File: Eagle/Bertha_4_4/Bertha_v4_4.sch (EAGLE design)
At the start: 115 parts, among them CON1 JACK_DC_BARREL, CON2 JACK_DC_BARREL, IC1 MCP1703DB, J1 RJ12RIGHTANGLE-I2C, J2 RJ12RIGHTANGLE-I2C, Q1 BSP75, Q2 BSP75, Q3 BSP75, Q4 BSP75, Q5 BSP75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

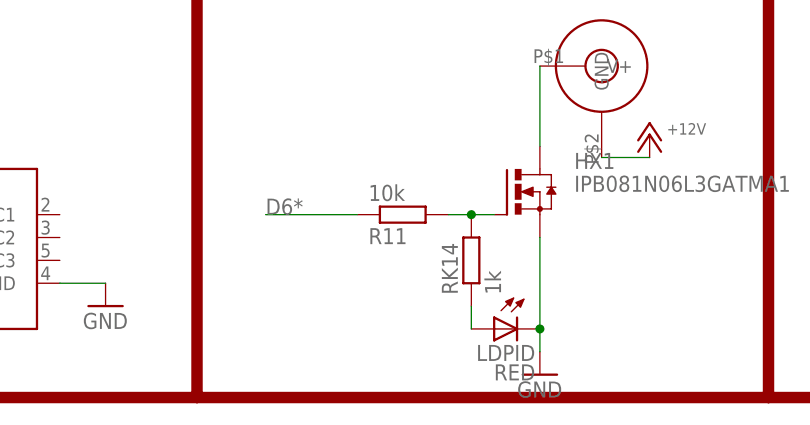
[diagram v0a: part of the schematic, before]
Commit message: correted PID diode, 4.5 finished, closes #72, ref #47
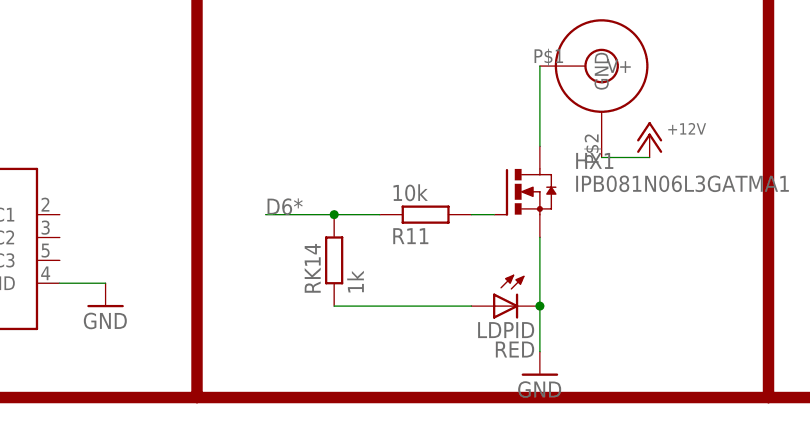
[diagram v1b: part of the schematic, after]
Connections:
- removed net N$6: HX1.G, R11.2, RK14.2
- new net N$4: HX1.G, R11.2
- net D6*: now also RK14.2
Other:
- moved on the sheet: LDPID, R11, RK14
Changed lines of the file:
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@@
 <?xml version="1.0" encoding="utf-8"?>
 <!DOCTYPE eagle SYSTEM "eagle.dtd">
-<eagle version="7.5.0">
+<eagle version="6.5.0">
 <drawing>
 <settings>
@@
 <instance part="GND27" gate="1" x="337.82" y="266.7"/>
 <instance part="HX1" gate="G$1" x="358.14" y="30.48"/>
-<instance part="R11" gate="G$1" x="345.44" y="27.94" rot="MR180"/>
+<instance part="R11" gate="G$1" x="347.98" y="27.94" rot="MR180"/>
 <instance part="P+2" gate="1" x="372.872" y="36.83" smashed="yes">
 <attribute name="VALUE" x="374.777" y="36.83" size="1.27" layer="96"/>
@@
 <instance part="Q6" gate="G$1" x="78.74" y="53.34"/>
 <instance part="Q5" gate="G$1" x="78.74" y="27.94"/>
-<instance part="RK14" gate="G$1" x="353.06" y="22.86" rot="R90"/>
+<instance part="RK14" gate="G$1" x="337.82" y="22.86" rot="R90"/>
 <instance part="RK13" gate="G$1" x="68.58" y="20.32" rot="R90"/>
 <instance part="RK12" gate="G$1" x="71.12" y="45.72" rot="R90"/>
@@
 <instance part="P+7" gate="G$1" x="487.68" y="274.32"/>
 <instance part="GND66" gate="1" x="487.68" y="264.16"/>
-<instance part="LDPID" gate="G$1" x="355.6" y="15.24" rot="MR270"/>
+<instance part="LDPID" gate="G$1" x="355.6" y="17.78" rot="MR270"/>
 <instance part="STEPPER" gate="G$1" x="497.84" y="119.38" rot="R180"/>
 <instance part="LDIN" gate="G$1" x="76.2" y="40.64" rot="MR270"/>
@@
 <pinref part="HX1" gate="G$1" pin="S"/>
 <pinref part="GND2" gate="1" pin="GND"/>
-<wire x1="360.68" y1="25.4" x2="360.68" y2="15.24" width="0.1524" layer="91"/>
+<wire x1="360.68" y1="25.4" x2="360.68" y2="17.78" width="0.1524" layer="91"/>
 <pinref part="LDPID" gate="G$1" pin="C"/>
-<wire x1="360.68" y1="15.24" x2="360.68" y2="12.7" width="0.1524" layer="91"/>
-<junction x="360.68" y="15.24"/>
+<wire x1="360.68" y1="17.78" x2="360.68" y2="12.7" width="0.1524" layer="91"/>
+<junction x="360.68" y="17.78"/>
 </segment>
 <segment>
@@
 <segment>
 <pinref part="R11" gate="G$1" pin="1"/>
-<wire x1="340.36" y1="27.94" x2="330.2" y2="27.94" width="0.1524" layer="91"/>
+<wire x1="342.9" y1="27.94" x2="337.82" y2="27.94" width="0.1524" layer="91"/>
 <label x="330.2" y="27.94" size="1.778" layer="95"/>
+<pinref part="RK14" gate="G$1" pin="2"/>
+<wire x1="337.82" y1="27.94" x2="330.2" y2="27.94" width="0.1524" layer="91"/>
+<junction x="337.82" y="27.94"/>
 </segment>
 </net>
@@
 </segment>
 </net>
-<net name="N$6" class="0">
-<segment>
-<pinref part="R11" gate="G$1" pin="2"/>
-<pinref part="HX1" gate="G$1" pin="G"/>
-<wire x1="350.52" y1="27.94" x2="353.06" y2="27.94" width="0.1524" layer="91"/>
-<pinref part="RK14" gate="G$1" pin="2"/>
-<wire x1="353.06" y1="27.94" x2="355.6" y2="27.94" width="0.1524" layer="91"/>
-<junction x="353.06" y="27.94"/>
-</segment>
-</net>
 <net name="N$3" class="0">
 <segment>
@@
 <segment>
 <pinref part="RK14" gate="G$1" pin="1"/>
-<wire x1="353.06" y1="15.24" x2="353.06" y2="17.78" width="0.1524" layer="91"/>
+<wire x1="353.06" y1="17.78" x2="337.82" y2="17.78" width="0.1524" layer="91"/>
 <pinref part="LDPID" gate="G$1" pin="A"/>
 </segment>
@@
 </segment>
 </net>
+<net name="N$4" class="0">
+<segment>
+<pinref part="HX1" gate="G$1" pin="G"/>
+<pinref part="R11" gate="G$1" pin="2"/>
+<wire x1="353.06" y1="27.94" x2="355.6" y2="27.94" width="0.1524" layer="91"/>
+</segment>
+</net>

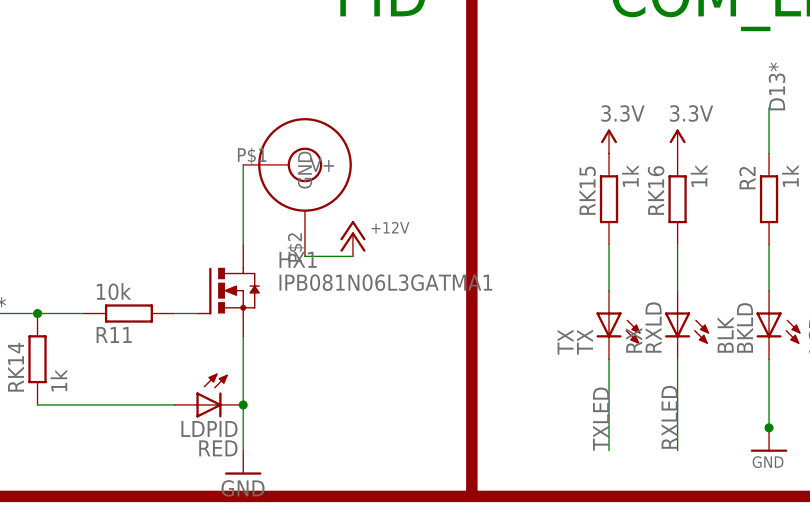
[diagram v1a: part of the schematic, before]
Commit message: corrected powerFET labelling
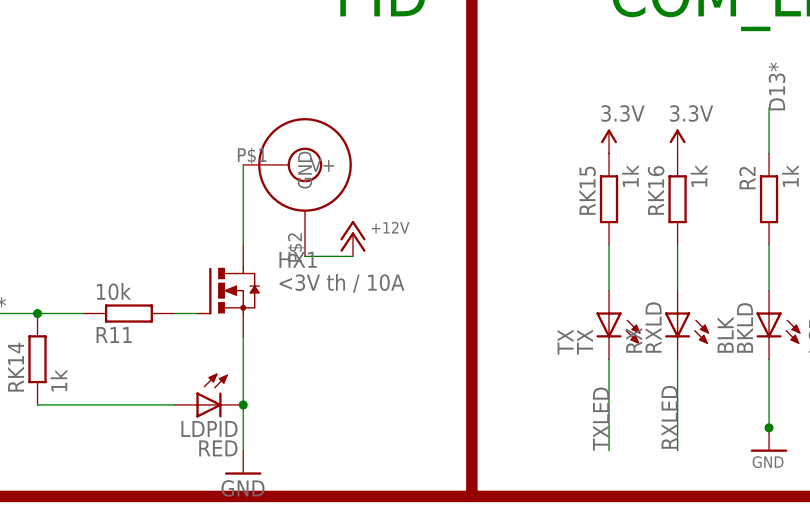
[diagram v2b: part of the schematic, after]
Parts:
- HX1: value IPB081N06L3GATMA1 -> <3V th / 10A
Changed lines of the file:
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@@
 <part name="GND8" library="supply1" deviceset="GND" device=""/>
 <part name="GND27" library="supply1" deviceset="GND" device=""/>
-<part name="HX1" library="transistor-power" deviceset="IRF3704" device="S" value="IPB081N06L3GATMA1"/>
+<part name="HX1" library="transistor-power" deviceset="IRF3704" device="S" value="&lt;3V th / 10A"/>
 <part name="R11" library="rcl" deviceset="R-EU_" device="R0805" value="10k"/>
 <part name="P+2" library="supply1" deviceset="+12V" device=""/>

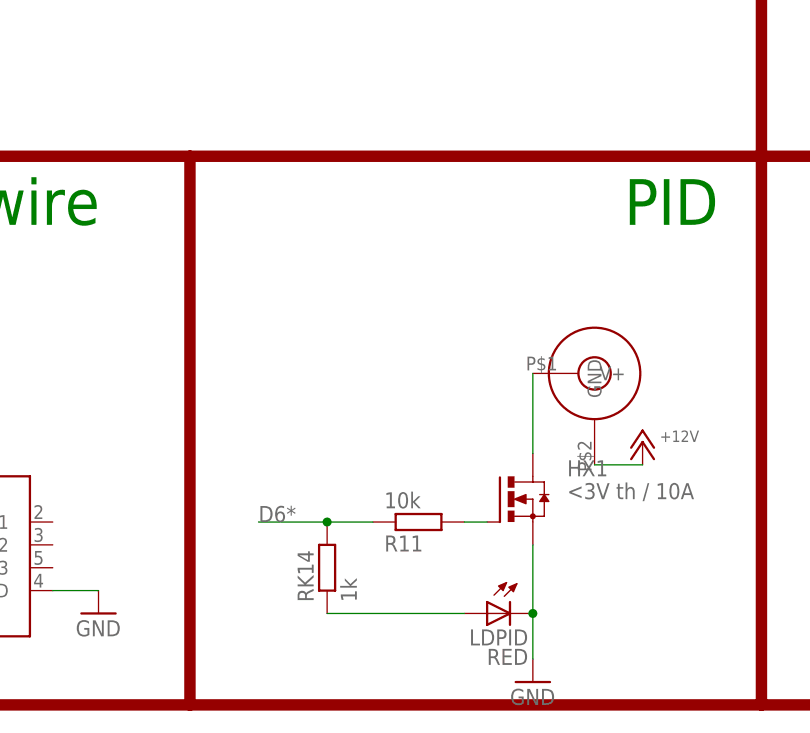
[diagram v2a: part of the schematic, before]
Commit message: added high side power switch with 5.6V zener on V4.5, drafted hack modif on 4.4, To be tested
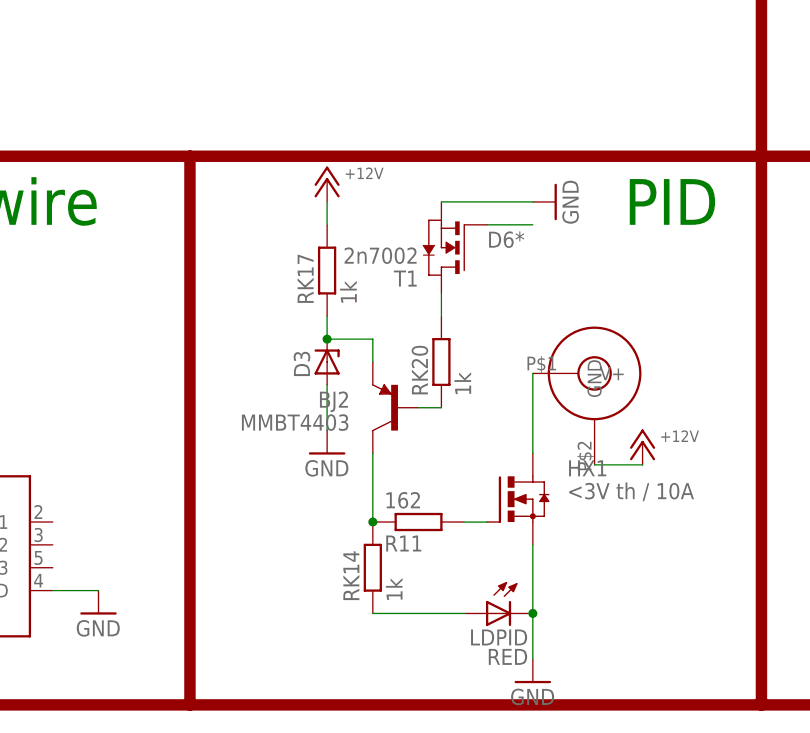
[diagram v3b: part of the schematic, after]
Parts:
- added BJ2: MMBT4403, SparkFun-DiscreteSemi:TRANSISTOR_PNPMMBT4403
- added D3: (no value), diode:ZENER-DIODEF126-10
- added RK17, RK20: 1k, rcl:R-EU_R0805
- added T1: 2n7002, zetex:NMOSSOT23
- R11: value 10k -> 162
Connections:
- new net N$10: BJ2.E, D3.C, RK17.1
- new net N$12: BJ2.B, RK20.1
- new net N$29: RK20.2, T1.D
- new net N$6: BJ2.C, R11.1, RK14.2
- net +12V: now also RK17.2
- net D6*: now also T1.G; no longer R11.1, RK14.2
- net GND: now also D3.A, T1.S
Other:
- moved on the sheet: RK14
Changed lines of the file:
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@@
 <part name="GND27" library="supply1" deviceset="GND" device=""/>
 <part name="HX1" library="transistor-power" deviceset="IRF3704" device="S" value="&lt;3V th / 10A"/>
-<part name="R11" library="rcl" deviceset="R-EU_" device="R0805" value="10k"/>
+<part name="R11" library="rcl" deviceset="R-EU_" device="R0805" value="162"/>
 <part name="P+2" library="supply1" deviceset="+12V" device=""/>
 <part name="GND2" library="supply1" deviceset="GND" device=""/>
@@
 <part name="X1" library="con-lumberg" deviceset="1503_09" device=""/>
 <part name="U$2" library="lpatiny" deviceset="DS18B20" device="SMALL" value="DS18B20"/>
+<part name="P+12" library="supply1" deviceset="+12V" device=""/>
+<part name="BJ2" library="SparkFun-DiscreteSemi" deviceset="TRANSISTOR_PNP" device="MMBT4403" value="MMBT4403"/>
+<part name="GND5" library="supply1" deviceset="GND" device=""/>
+<part name="D3" library="diode" deviceset="ZENER-DIODE" device="F126-10"/>
+<part name="RK17" library="rcl" deviceset="R-EU_" device="R0805" value="1k"/>
+<part name="T1" library="zetex" deviceset="NMOSSOT23" device="" value="2n7002"/>
+<part name="RK20" library="rcl" deviceset="R-EU_" device="R0805" value="1k"/>
+<part name="GND9" library="supply1" deviceset="GND" device=""/>
 </parts>
 <sheets>
@@
 <instance part="Q6" gate="G$1" x="78.74" y="53.34"/>
 <instance part="Q5" gate="G$1" x="78.74" y="27.94"/>
-<instance part="RK14" gate="G$1" x="337.82" y="22.86" rot="R90"/>
+<instance part="RK14" gate="G$1" x="342.9" y="22.86" rot="R90"/>
 <instance part="RK13" gate="G$1" x="68.58" y="20.32" rot="R90"/>
 <instance part="RK12" gate="G$1" x="71.12" y="45.72" rot="R90"/>
@@
 <instance part="X1" gate="G$1" x="284.48" y="43.18" rot="MR180"/>
 <instance part="U$2" gate="G$1" x="297.18" y="22.86"/>
+<instance part="P+12" gate="1" x="337.82" y="66.04" smashed="yes">
+<attribute name="VALUE" x="339.725" y="66.04" size="1.27" layer="96"/>
+</instance>
+<instance part="BJ2" gate="G$1" x="345.44" y="40.64" rot="MR0"/>
+<instance part="GND5" gate="1" x="337.82" y="35.56"/>
+<instance part="D3" gate="G$1" x="337.82" y="45.72" rot="R90"/>
+<instance part="RK17" gate="G$1" x="337.82" y="55.88" rot="R90"/>
+<instance part="T1" gate="A" x="350.52" y="58.42" rot="R180"/>
+<instance part="RK20" gate="G$1" x="350.52" y="45.72" rot="R90"/>
+<instance part="GND9" gate="1" x="363.22" y="63.5" rot="R90"/>
 </instances>
 <busses>
@@
 <wire x1="274.32" y1="38.1" x2="279.4" y2="38.1" width="0.1524" layer="91"/>
 </segment>
+<segment>
+<pinref part="D3" gate="G$1" pin="A"/>
+<pinref part="GND5" gate="1" pin="GND"/>
+<wire x1="337.82" y1="38.1" x2="337.82" y2="43.18" width="0.1524" layer="91"/>
+</segment>
+<segment>
+<pinref part="T1" gate="A" pin="S"/>
+<pinref part="GND9" gate="1" pin="GND"/>
+<wire x1="360.68" y1="63.5" x2="350.52" y2="63.5" width="0.1524" layer="91"/>
+</segment>
 </net>
 <net name="SCK" class="0">
@@
 </segment>
 <segment>
-<pinref part="R11" gate="G$1" pin="1"/>
-<wire x1="342.9" y1="27.94" x2="337.82" y2="27.94" width="0.1524" layer="91"/>
-<label x="330.2" y="27.94" size="1.778" layer="95"/>
-<pinref part="RK14" gate="G$1" pin="2"/>
-<wire x1="337.82" y1="27.94" x2="330.2" y2="27.94" width="0.1524" layer="91"/>
-<junction x="337.82" y="27.94"/>
+<pinref part="T1" gate="A" pin="G"/>
+<wire x1="355.6" y1="60.96" x2="360.68" y2="60.96" width="0.1524" layer="91"/>
+<label x="355.6" y="58.42" size="1.778" layer="95"/>
 </segment>
 </net>
@@
 <junction x="165.1" y="243.84"/>
 </segment>
+<segment>
+<pinref part="P+12" gate="1" pin="+12V"/>
+<pinref part="RK17" gate="G$1" pin="2"/>
+<wire x1="337.82" y1="63.5" x2="337.82" y2="60.96" width="0.1524" layer="91"/>
+</segment>
 </net>
 <net name="3.3V" class="1">
@@
 <segment>
 <pinref part="RK14" gate="G$1" pin="1"/>
-<wire x1="353.06" y1="17.78" x2="337.82" y2="17.78" width="0.1524" layer="91"/>
+<wire x1="353.06" y1="17.78" x2="342.9" y2="17.78" width="0.1524" layer="91"/>
 <pinref part="LDPID" gate="G$1" pin="A"/>
 </segment>
@@
 </segment>
 </net>
+<net name="N$6" class="0">
+<segment>
+<pinref part="RK14" gate="G$1" pin="2"/>
+<pinref part="R11" gate="G$1" pin="1"/>
+<pinref part="BJ2" gate="G$1" pin="C"/>
+<wire x1="342.9" y1="35.56" x2="342.9" y2="27.94" width="0.1524" layer="91"/>
+<junction x="342.9" y="27.94"/>
+</segment>
+</net>
+<net name="N$10" class="0">
+<segment>
+<pinref part="RK17" gate="G$1" pin="1"/>
+<pinref part="D3" gate="G$1" pin="C"/>
+<wire x1="337.82" y1="48.26" x2="337.82" y2="50.8" width="0.1524" layer="91"/>
+<wire x1="337.82" y1="48.26" x2="342.9" y2="48.26" width="0.1524" layer="91"/>
+<junction x="337.82" y="48.26"/>
+<pinref part="BJ2" gate="G$1" pin="E"/>
+<wire x1="342.9" y1="48.26" x2="342.9" y2="45.72" width="0.1524" layer="91"/>
+</segment>
+</net>
+<net name="N$12" class="0">
+<segment>
+<pinref part="BJ2" gate="G$1" pin="B"/>
+<wire x1="347.98" y1="40.64" x2="350.52" y2="40.64" width="0.1524" layer="91"/>
+<pinref part="RK20" gate="G$1" pin="1"/>
+</segment>
+</net>
+<net name="N$29" class="0">
+<segment>
+<pinref part="RK20" gate="G$1" pin="2"/>
+<pinref part="T1" gate="A" pin="D"/>
+<wire x1="350.52" y1="50.8" x2="350.52" y2="53.34" width="0.1524" layer="91"/>
+</segment>
+</net>
